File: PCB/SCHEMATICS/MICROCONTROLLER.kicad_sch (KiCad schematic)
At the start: 0 parts

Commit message: Updated Schematics
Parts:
- added C6: 3.3nF, symbol Device:C_Small
- added U4: ~, symbol DEBUGGER:DEBUGGER
- added U5: ~, symbol DEBUGGER:Micro_usb
- added U6: 24LC08, symbol Memory_EEPROM:24LC08
- added U7: ~, symbol DEBUGGER:FTDI_header
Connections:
- new net: U4.3 (USB_D-), U5.2 (D-)
- new net: U4.4 (USB_D+), U5.3 (D+)
- new net +3.3V: U4.2 (Vtarget), U7.3
- new net 3V3: C6.1, U6.7 (WP), U6.8 (VCC)
- new net 5V: U4.1 (5V), U5.1 (VBUS), U7.2
- new net GND: C6.2, U4.5 (GND), U5.5 (GND), U5.6 (SH1), U5.7 (SH2), U5.8 (SH3), U5.9 (SH4), U6.1 (A0), U6.2 (A1), U6.3 (A2), U6.4 (GND), U7.6
- new net NRST: U4.6 (NRST)
- new net PA10: U6.5 (SDA)
- new net PA11: U7.4
- new net PA7: U7.5
- new net PA8: U7.1
- new net PA9: U6.6 (SCL)
- new net T_SWCLK: U4.7 (SWCLK)
- new net T_SWDIO: U4.8 (SWDIO)
- no-connect marks 0 -> 1
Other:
- note added: "EPROM"

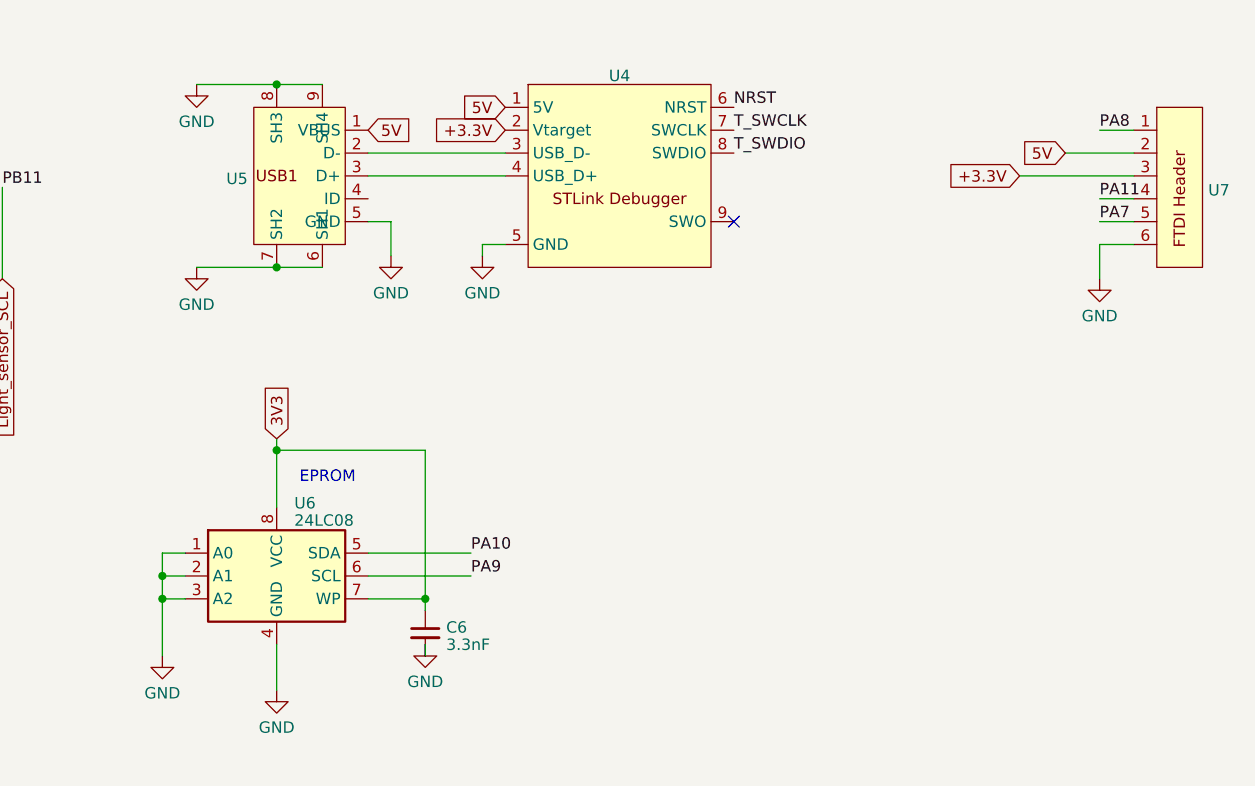
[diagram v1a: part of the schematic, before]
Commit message: UPDATED SCHEMATICS.
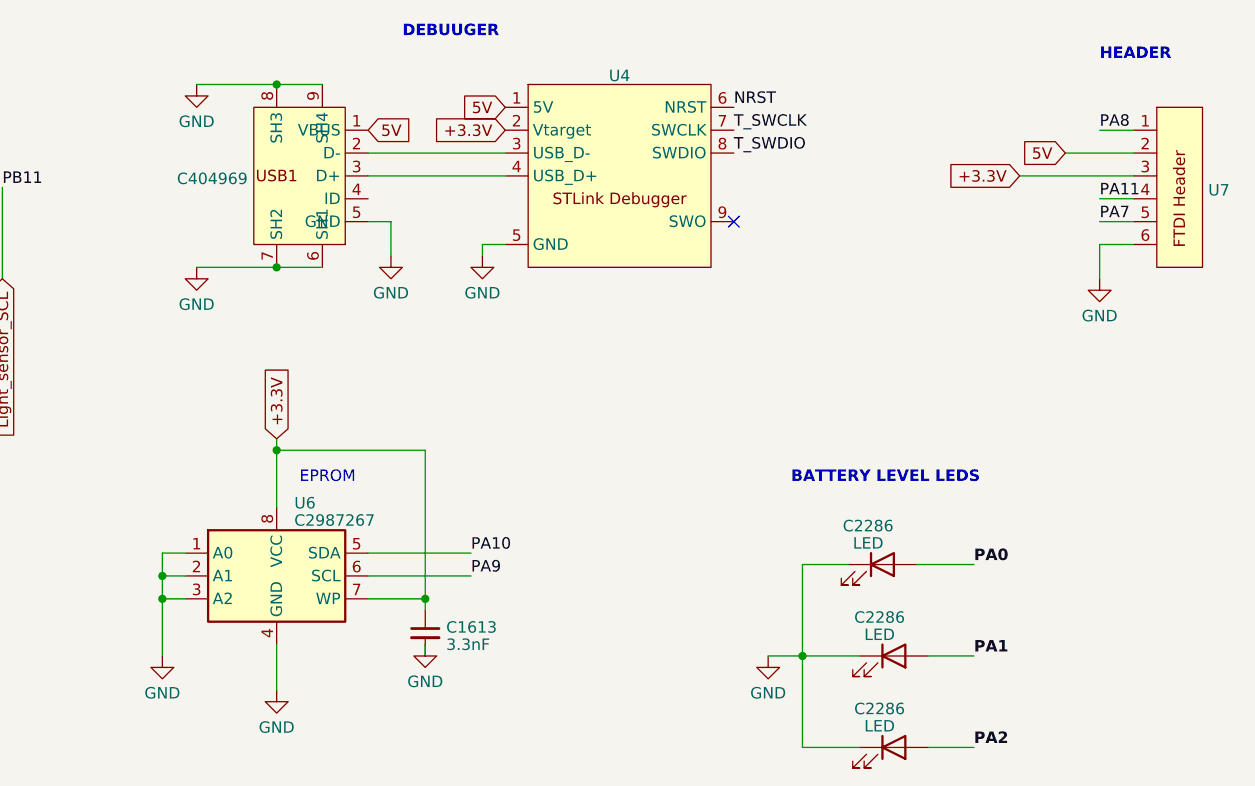
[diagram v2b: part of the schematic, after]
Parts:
- added C2286 (x3): LED, symbol Device:LED
- C1613: renamed from C6; Unit Price (none) -> 0.0058
- C404969: renamed from U5; Unit Price (none) -> 0.0333
- U6: value 24LC08 -> C2987267; Extended (none) -> YES; Unit Price (none) -> 0.0920
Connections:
- net 3V3 is gone; now on net +3.3V: C1613.1, U6.7 (WP), U6.8 (VCC)
- net GND: now also C2286.1 (K), C2286.1 (K), C2286.1 (K)
- new net PA0: C2286.2 (A)
- new net PA1: C2286.2 (A)
- new net PA2: C2286.2 (A)
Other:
- note added: "BATTERY LEVEL LEDS"
- note added: "DEBUUGER"
- note added: "HEADER"

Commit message: Adjusted Schematics
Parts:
- removed U4: ~, symbol DEBUGGER:DEBUGGER
- added C17520 (x2): 2.2k, symbol Device:R_Small_US
- added TP22, TP23, TP24, TP25, TP26, TP27: TestPoint, symbol Connector:TestPoint
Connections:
- net +3.3V: now also TP25.1
- net 5V: now also TP22.1
- net GND: now also C404969.4 (ID)
- net PA10: now also C17520.2, TP26.1
- net PA9: now also C17520.2, TP27.1
- net at C404969.2 (D-): now also C17520.1, TP23.1
- net at C404969.3 (D+): now also C17520.1, TP24.1
- no-connect marks 1 -> 0
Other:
- note added: "Micro USB"
- note removed: "DEBUUGER"
- moved on the sheet: C1613, U6, U7

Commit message: Updated schematics
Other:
- company: (none) -> UCT
- title: (none) -> MICROCONTROLLER
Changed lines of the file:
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@@
 (kicad_sch (version 20230121) (generator eeschema)
   (paper "A4")
+  (title_block
+    (title "MICROCONTROLLER")
+    (company "UCT")
+    (comment 1 "Author: Murray Inglis")
+    (comment 2 "Version: 2")
+  )
   (junction (at 152.4 107.95) (diameter 0) (color 0 0 0 0)
   )

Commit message: Updated schematics
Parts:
- added C6 (x13): 0, symbol Device:R_Small_US
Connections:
- net 3V3: now also C6.1, C6.2
- net 5V: now also C6.1; no longer U7.2
- net PA0: now also C6.2; no longer C2286.2 (A)
- net PA1: now also C6.2; no longer C2286.2 (A)
- net PA10: now also C6.2, C6.2; no longer C17520.2, TP26.1, U6.5 (SDA)
- net PA11: now also C6.1; no longer U7.4
- net PA2: now also C6.2; no longer C2286.2 (A)
- net PA7: now also C6.1; no longer U7.5
- net PA8: now also C6.1; no longer U7.1
- net PA9: now also C6.2, C6.2; no longer C17520.2, TP27.1, U6.6 (SCL)
- net +3.3V: no longer names the net of C1613.1, TP25.1, U6.7 (WP), U6.8 (VCC)
- net +3.3V: now also C6.1; no longer U7.3
- new net: C2286.2 (A), C6.1 (x3)
- new net: C6.2, U7.4
- new net: C17520.2, C6.1 (x2)
- new net: C6.1, TP26.1, U6.5 (SDA)
- new net: C6.1, TP27.1, U6.6 (SCL)
- new net: C6.2, U7.5
- new net: C6.2, U7.2
- new net: C6.2, U7.1
- new net: C6.2, U7.3

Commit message: Updated BOM
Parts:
- C6: PART  (none) -> C4177; Unit Price (none) -> 0.0012
- C6: renamed from C1613; PART  (none) -> C1613
- D6, D7, D8: renamed from C2286; PART  (none) -> C2286
- MicroXNJ: renamed from C404969; Extended (none) -> YES; PART  (none) -> C404969
- R25, R27: renamed from C17520; PART  (none) -> C17520; Unit Price (none) -> 0.0017
- TP22: PART  (none) -> TP22
- TP23: PART  (none) -> TP23
- TP24: PART  (none) -> TP24
- TP25: PART  (none) -> TP25
- TP26: PART  (none) -> TP26
- TP27: PART  (none) -> TP27
- U6: PART  (none) -> C2987267
- U7: value ~ -> FTDI; PART  (none) -> U7
